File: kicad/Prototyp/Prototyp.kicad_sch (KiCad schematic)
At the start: 16 parts

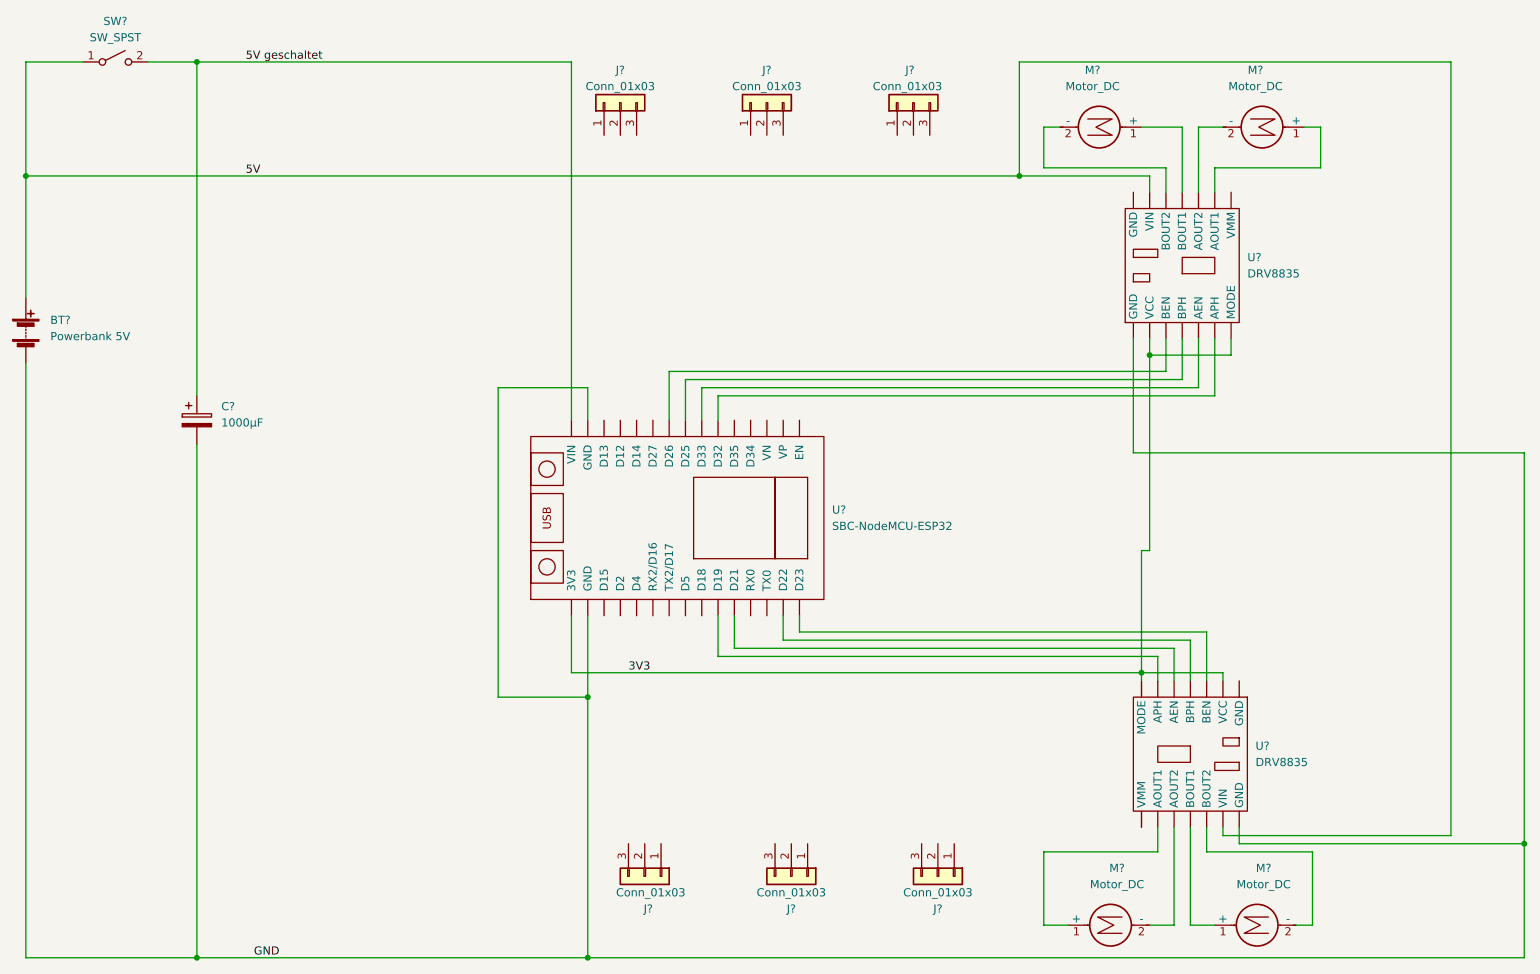
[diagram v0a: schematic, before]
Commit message: Schaltplan mit Servos fertiggestellt
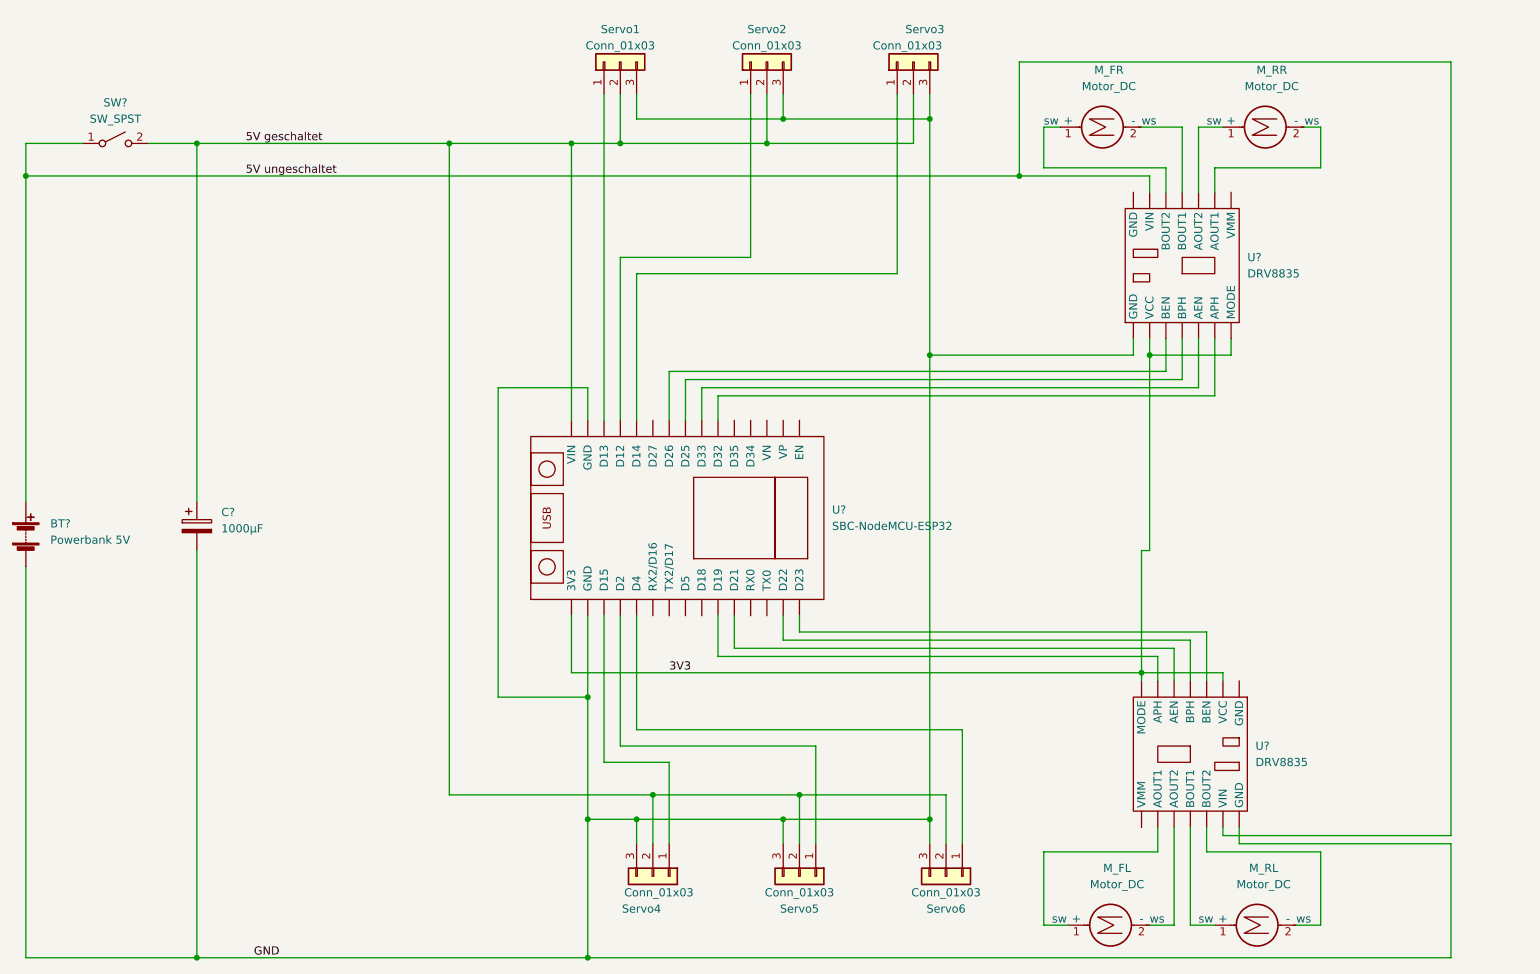
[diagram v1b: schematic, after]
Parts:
- gave numbers to parts that had none: 10
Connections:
- net 5V geschaltet: now also Servo1.2 (Pin_2), Servo2.2 (Pin_2), Servo3.2 (Pin_2), Servo4.2 (Pin_2), Servo5.2 (Pin_2), Servo6.2 (Pin_2)
- net GND: now also Servo1.3 (Pin_3), Servo2.3 (Pin_3), Servo3.3 (Pin_3), Servo4.3 (Pin_3), Servo5.3 (Pin_3), Servo6.3 (Pin_3)
- net at Servo2.1 (Pin_1): now also U?. (VP)
- net at Servo3.1 (Pin_1): now also U?. (VP)
- net at Servo6.1 (Pin_1): now also U?. (VP)
- net at Servo5.1 (Pin_1): now also U?. (VP)
- net at Servo1.1 (Pin_1): now also U?. (VP)
- net at Servo4.1 (Pin_1): now also U?. (VP)
- net 5V renamed 5V ungeschaltet
- new net: U?. (VMM), U?. (VP) (x8)
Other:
- note added: "sw"
- note added: "ws"
- title: (none) -> Mecanum Roboter
- moved on the sheet: BT?, C?, M_FR, M_RR, SW?, Servo1, Servo2, Servo3, Servo4, Servo5, Servo6

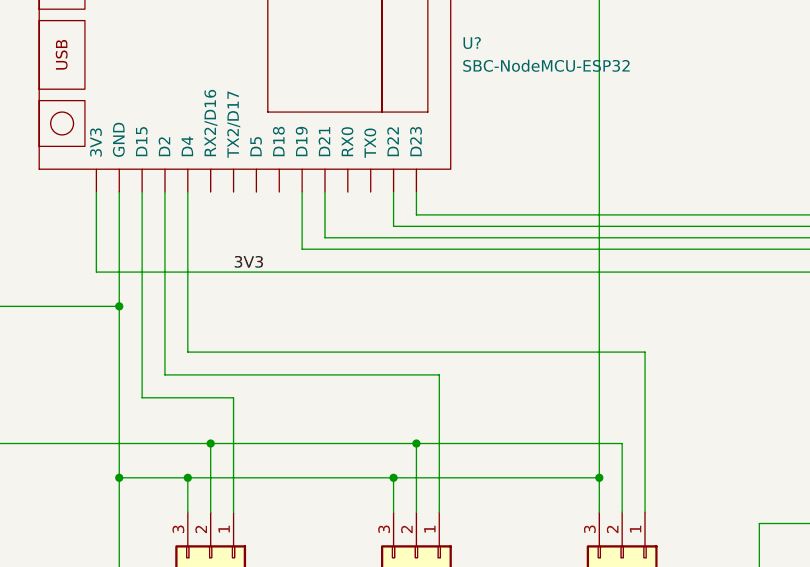
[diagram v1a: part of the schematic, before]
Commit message: Gamecontroller-Sketch hinzugefügt
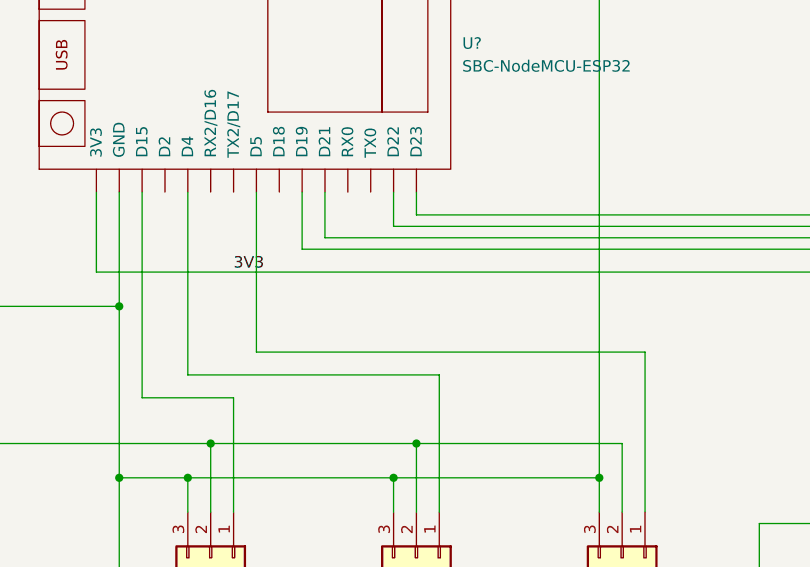
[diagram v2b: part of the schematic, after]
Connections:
- new net: U?. (VMM), U?. (VP) (x8)
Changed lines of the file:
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@@
-    (stroke (width 0) (type default) (color 0 0 0 0))
-  )
-  (wire (pts (xy 133.35 125.73) (xy 184.15 125.73))
     (stroke (width 0) (type default) (color 0 0 0 0))
   )
@@
     (stroke (width 0) (type default) (color 0 0 0 0))
   )
+  (wire (pts (xy 140.97 125.73) (xy 184.15 125.73))
+    (stroke (width 0) (type default) (color 0 0 0 0))
+  )
   (wire (pts (xy 215.9 69.85) (xy 215.9 64.77))
     (stroke (width 0) (type default) (color 0 0 0 0))
@@
     (stroke (width 0) (type default) (color 0 0 0 0))
   )
+  (wire (pts (xy 133.35 128.27) (xy 161.29 128.27))
+    (stroke (width 0) (type default) (color 0 0 0 0))
+  )
+  (wire (pts (xy 133.35 107.95) (xy 133.35 128.27))
+    (stroke (width 0) (type default) (color 0 0 0 0))
+  )
   (wire (pts (xy 138.43 130.81) (xy 138.43 143.51))
     (stroke (width 0) (type default) (color 0 0 0 0))
@@
     (stroke (width 0) (type default) (color 0 0 0 0))
   )
-  (wire (pts (xy 130.81 107.95) (xy 130.81 128.27))
-    (stroke (width 0) (type default) (color 0 0 0 0))
-  )
   (wire (pts (xy 227.33 143.51) (xy 260.35 143.51))
     (stroke (width 0) (type default) (color 0 0 0 0))
@@
     (stroke (width 0) (type default) (color 0 0 0 0))
   )
-  (wire (pts (xy 133.35 107.95) (xy 133.35 125.73))
-    (stroke (width 0) (type default) (color 0 0 0 0))
-  )
   (wire (pts (xy 125.73 120.65) (xy 111.76 120.65))
     (stroke (width 0) (type default) (color 0 0 0 0))
@@
     (stroke (width 0) (type default) (color 0 0 0 0))
   )
-  (wire (pts (xy 130.81 128.27) (xy 161.29 128.27))
-    (stroke (width 0) (type default) (color 0 0 0 0))
-  )
   (wire (pts (xy 222.25 144.78) (xy 240.03 144.78))
     (stroke (width 0) (type default) (color 0 0 0 0))
@@
     (stroke (width 0) (type default) (color 0 0 0 0))
   )
+  (wire (pts (xy 140.97 107.95) (xy 140.97 125.73))
+    (stroke (width 0) (type default) (color 0 0 0 0))
+  )
